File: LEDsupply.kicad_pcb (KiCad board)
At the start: 2 copper layers, 28.6 x 18 mm, 16 parts, among them U1 MIC2954, U2 MCP4018-502

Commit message: Added a KK series connector
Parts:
- JP3: footprint Connector_PinHeader_2.54mm:PinHeader_1x03_P2.54mm_Vertical -> Connector_Molex:Molex_KK-254_AE-6410-03A_1x03_P2.54mm_Vertical; moved to F.Cu
- R5: moved to B.Cu
- moved JP3 5.75 mm to (143.5, 102.2), turned to 180 degrees
- moved R5 0.80 mm to (139.5, 99.7)
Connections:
- JP3 pad 1: /VREGOUT -> GND
- JP3 pad 3: GND -> /VREGOUT
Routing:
- net GND: track 46.4 -> 43.0 mm
- net /PWM: track 11.8 -> 10.9 mm

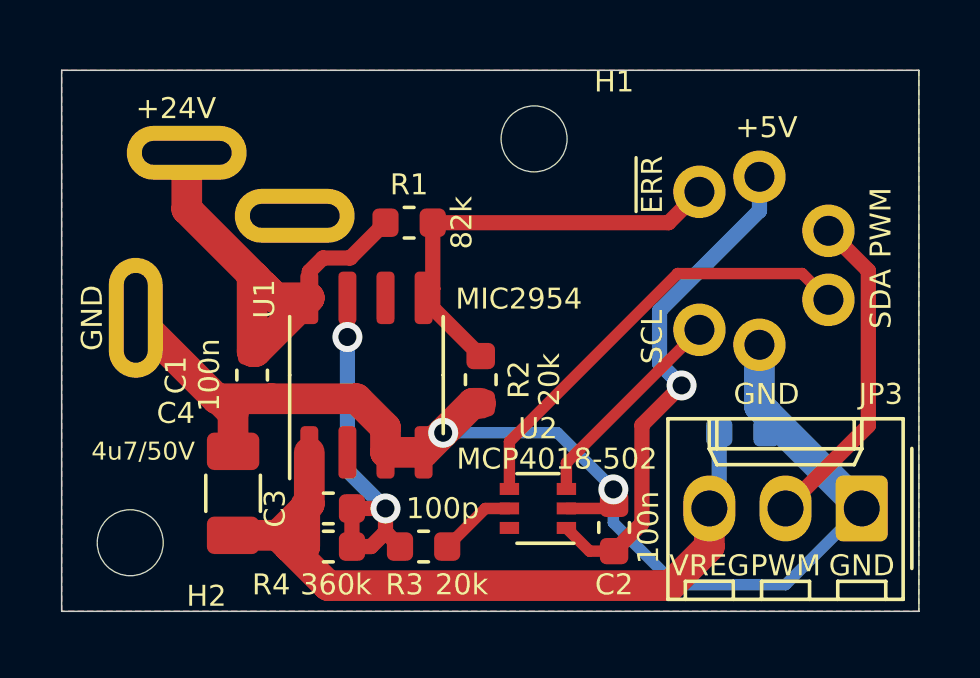
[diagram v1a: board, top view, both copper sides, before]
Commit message: Added I2C pullup resistors, fixed H1 label position, changed R4 from 20 to 24k
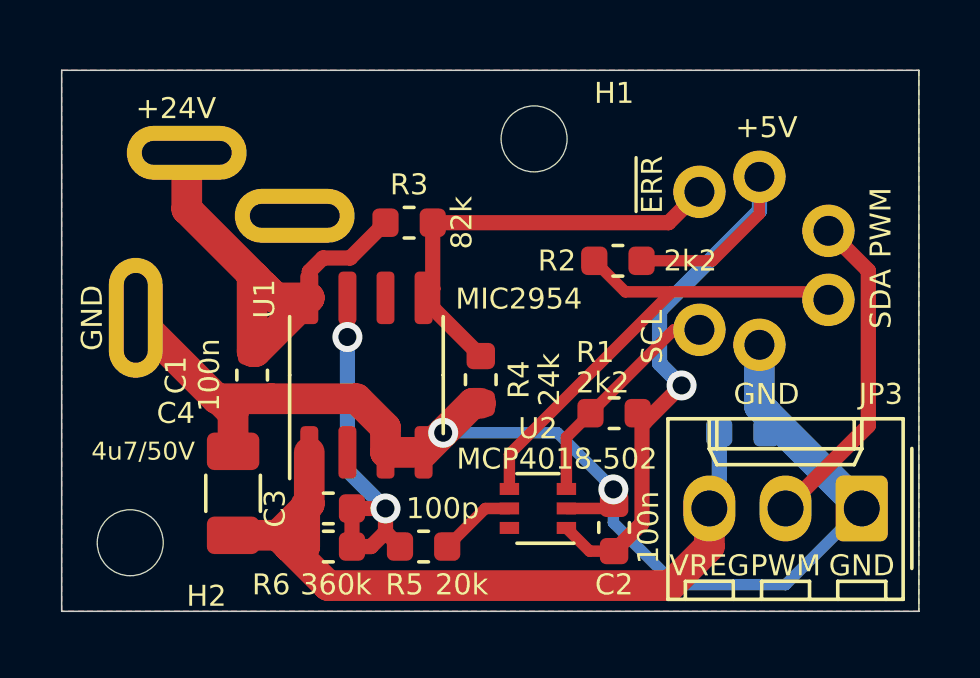
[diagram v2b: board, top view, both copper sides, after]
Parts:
- added R1: 2k2, Resistor_SMD:R_0603_1608Metric, F.Cu at (135.3, 99.1)
- added R2: 2k2, Resistor_SMD:R_0603_1608Metric, F.Cu at (135.4, 94.0)
- JP3: value Conn_01x03_Female -> KK_3way
- R4: renamed from R2; value 20k -> 24k
- renumbered JP2 to JP1, JP1 to JP2, R1 to R3, R3 to R5, R4 to R6, R5 to R7
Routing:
- net +5V: track 17.0 -> 23.2 mm
- net /SDA: track 14.9 -> 17.2 mm
